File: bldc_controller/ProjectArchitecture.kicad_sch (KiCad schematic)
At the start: 0 parts

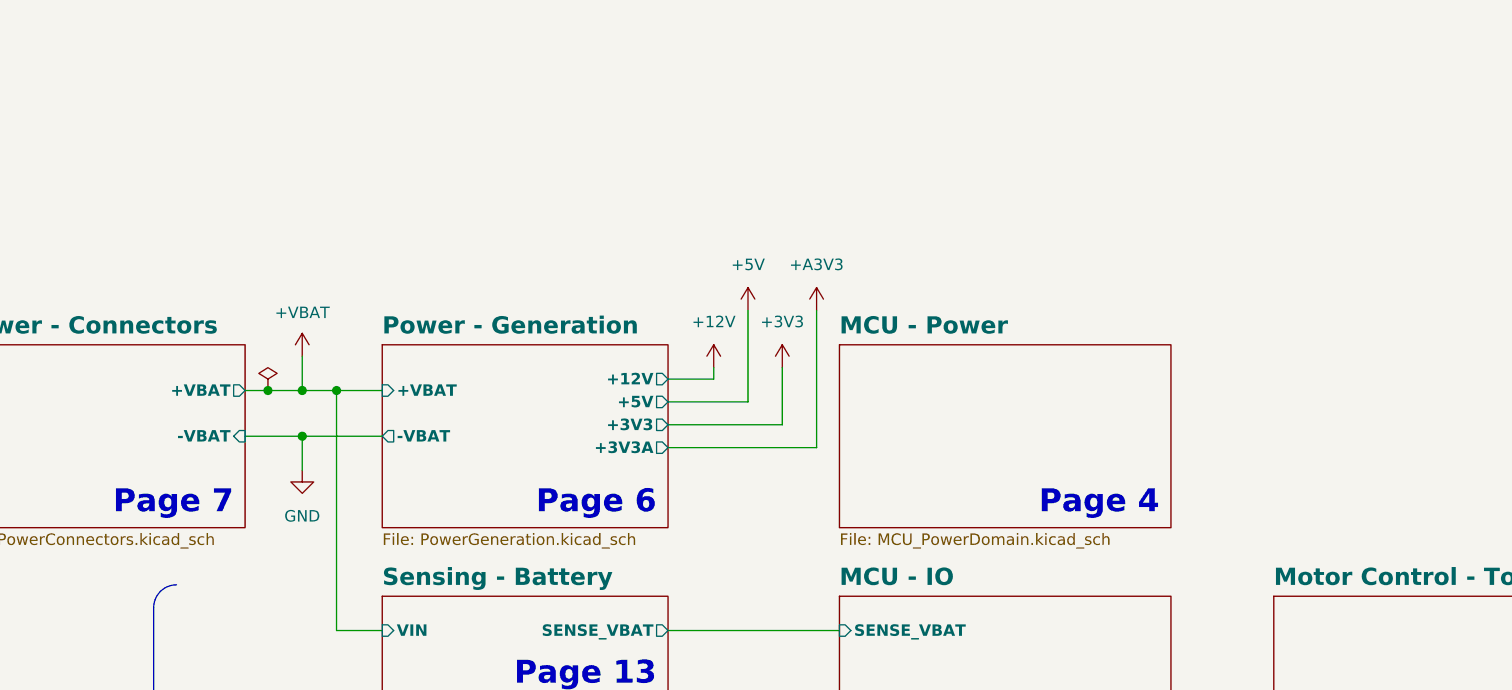
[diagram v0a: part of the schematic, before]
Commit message: added chassis connection to connector MP. Might need to change design rules to be compatible with low-cost PCBWay
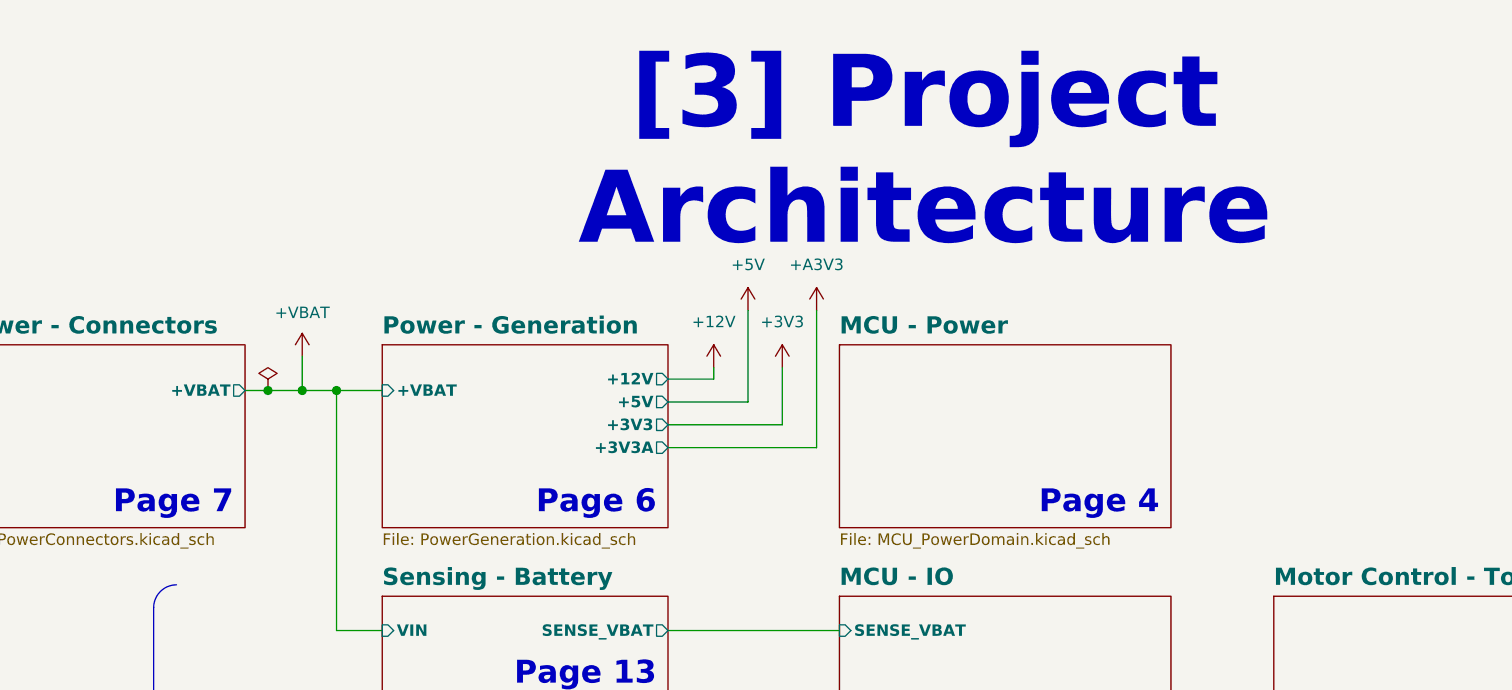
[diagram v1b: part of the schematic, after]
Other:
- sheet Power - Connectors ports: added none; removed -VBAT
- sheet Power - Generation ports: added none; removed -VBAT
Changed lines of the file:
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@@
   (junction (at 195.58 129.54) (diameter 0) (color 0 0 0 0)
-  )
-  (junction (at 140.97 58.42) (diameter 1.016) (color 0 0 0 1)
   )
   (junction (at 195.58 167.64) (diameter 0) (color 0 0 0 0)
@@
     (stroke (width 0) (type default))
   )
-  (wire (pts (xy 140.97 58.42) (xy 149.86 58.42))
-    (stroke (width 0.381) (type default) (color 0 0 0 1))
-  )
   (wire (pts (xy 181.61 101.6) (xy 193.04 101.6))
     (stroke (width 0) (type default))
@@
     (stroke (width 0) (type default))
   )
-  (wire (pts (xy 140.97 58.42) (xy 140.97 62.23))
-    (stroke (width 0.381) (type default) (color 0 0 0 1))
-  )
   (wire (pts (xy 149.86 125.73) (xy 140.97 125.73))
     (stroke (width 0) (type default))
@@
   (bus (pts (xy 181.61 167.64) (xy 195.58 167.64))
     (stroke (width 0) (type default))
-  )
-  (wire (pts (xy 134.62 58.42) (xy 140.97 58.42))
-    (stroke (width 0.381) (type default) (color 0 0 0 1))
   )
   (wire (pts (xy 149.86 134.62) (xy 138.43 134.62))
@@
     (effects (font (size 1.905 1.905) (thickness 0.381) bold (color 0 0 0 1)) (justify right top))
   )
+  (text_box "[3] Project Architecture"
+    (at 144.78 20.32 0) (size 130.81 12.7)
+    (stroke (width -0.0001) (type default))
+    (fill (type none))
+    (effects (font (face "Times New Roman") (size 8 8) (thickness 1.2) bold (color 162 22 34 1)))
+  )
   (text_box "LEDs, version"
     (at 299.085 165.735 0) (size 13.335 7.62)
@@
     )
   )
-  (symbol (lib_id "power:GND") (at 140.97 62.23 0) (unit 1)
-    (in_bom yes) (on_board yes) (dnp no) (fields_autoplaced)
-    (property "Reference" "#PWR03" (at 140.97 68.58 0)
-      (effects (font (size 1.27 1.27)) hide)
-    )
-    (property "Value" "GND" (at 140.97 67.31 0)
-      (effects (font (size 1.27 1.27)))
-    )
-    (property "Footprint" "" (at 140.97 62.23 0)
-      (effects (font (size 1.27 1.27)) hide)
-    )
-    (property "Datasheet" "" (at 140.97 62.23 0)
-      (effects (font (size 1.27 1.27)) hide)
-    )
-    (pin "1")
-    (instances
-      (project "bldc_controller"
-        (path "/0650c7a8-acba-429c-9f8e-eec0baf0bc1c"
-          (reference "#PWR03") (unit 1)
-        )
-        (path "/0650c7a8-acba-429c-9f8e-eec0baf0bc1c/fede4c36-00cc-4d3d-b71c-5243ba232202"
-          (reference "#PWR078") (unit 1)
-        )
-      )
-    )
-  )
   (sheet (at 248.92 173.99) (size 40.64 10.16) (fields_autoplaced)
     (stroke (width 0.1524) (type solid))
@@
       (effects (font (face "Arial") (size 1.27 1.27)) (justify left top))
     )
-    (pin "-VBAT" input (at 134.62 58.42 0)
-      (effects (font (size 1.27 1.27) (thickness 0.254) bold) (justify right))
-    )
     (pin "+VBAT" output (at 134.62 53.34 0)
       (effects (font (size 1.27 1.27) (thickness 0.254) bold) (justify right))
@@
       (effects (font (face "Arial") (size 1.27 1.27)) (justify left top))
     )
-    (pin "-VBAT" output (at 149.86 58.42 180)
-      (effects (font (size 1.27 1.27) (thickness 0.254) bold) (justify left))
-    )
     (pin "+VBAT" input (at 149.86 53.34 180)

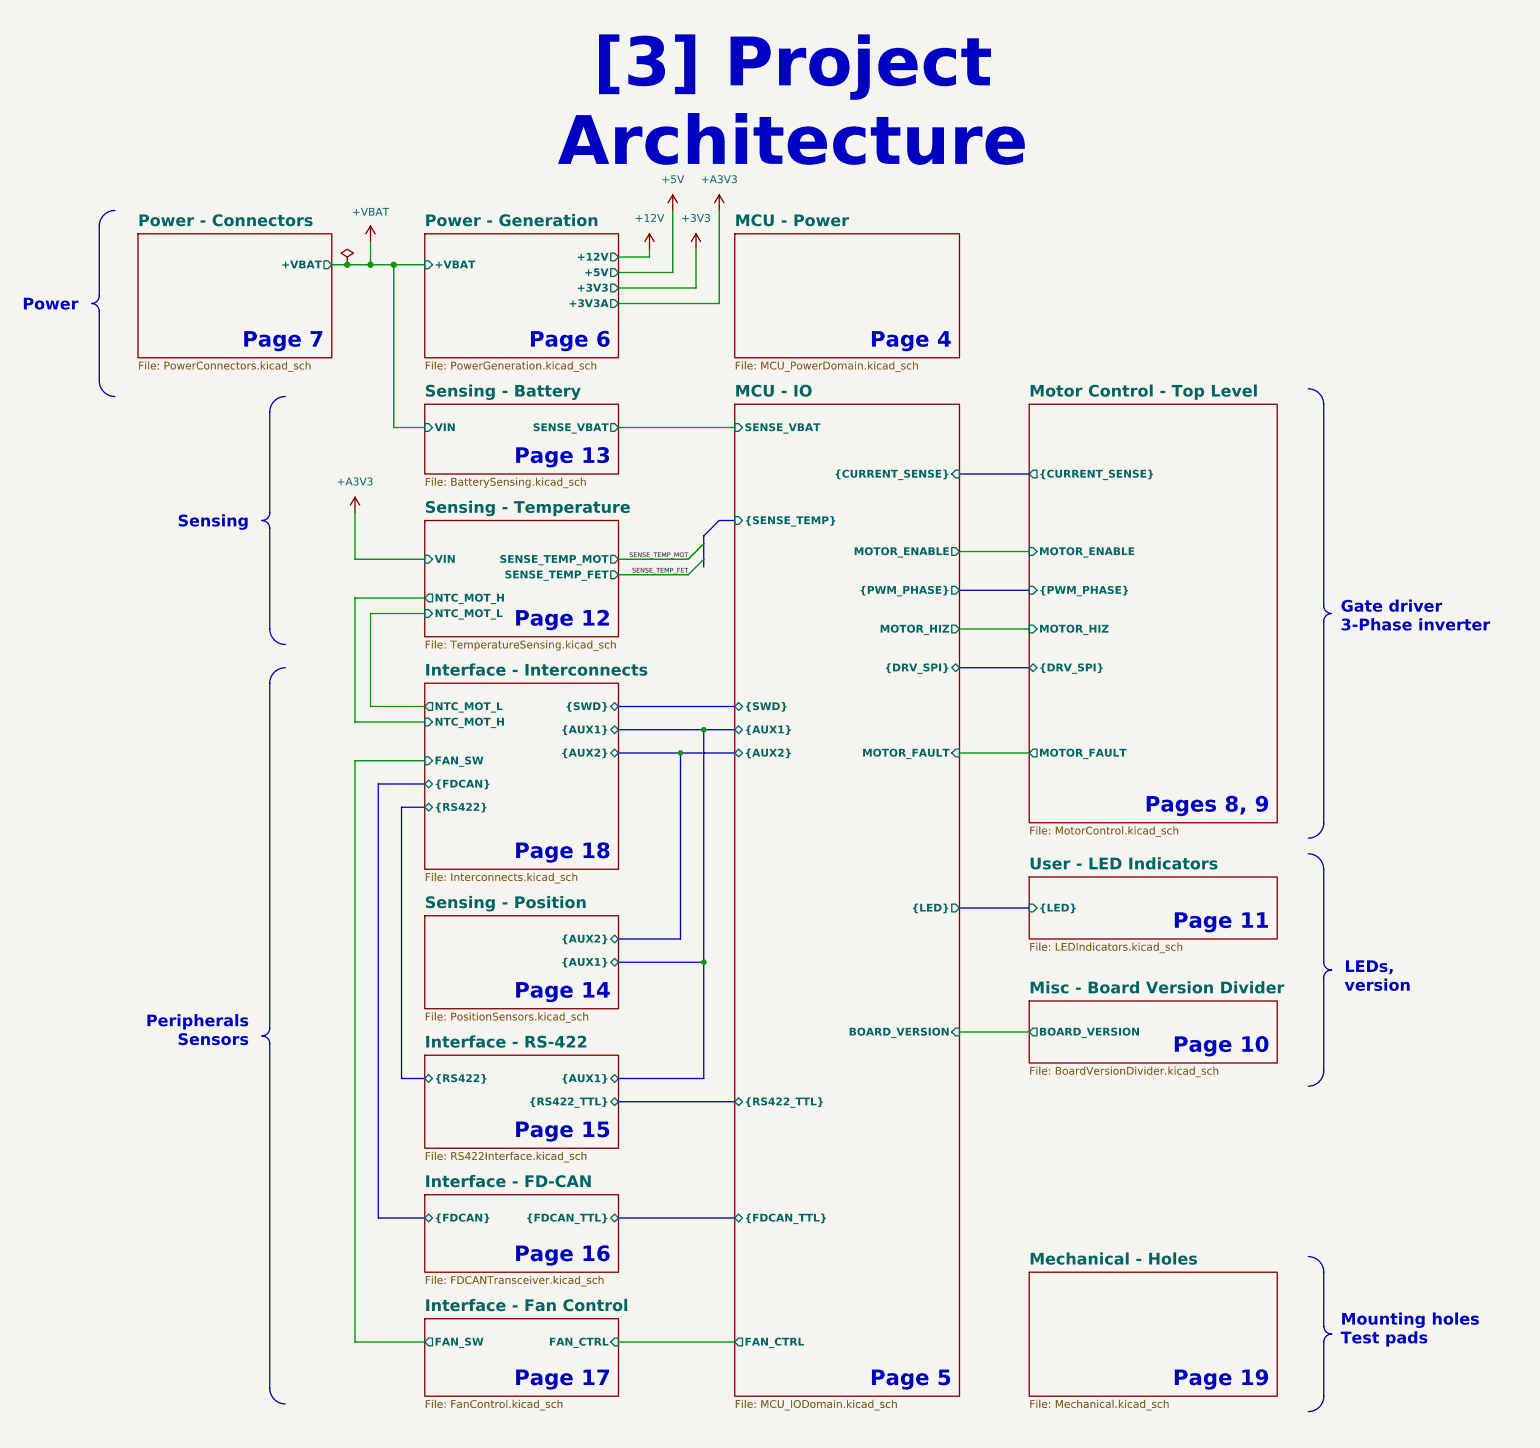
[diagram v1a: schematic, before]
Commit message: Replaced 3v3 buck with WSON package alternative. Will back-annotate components
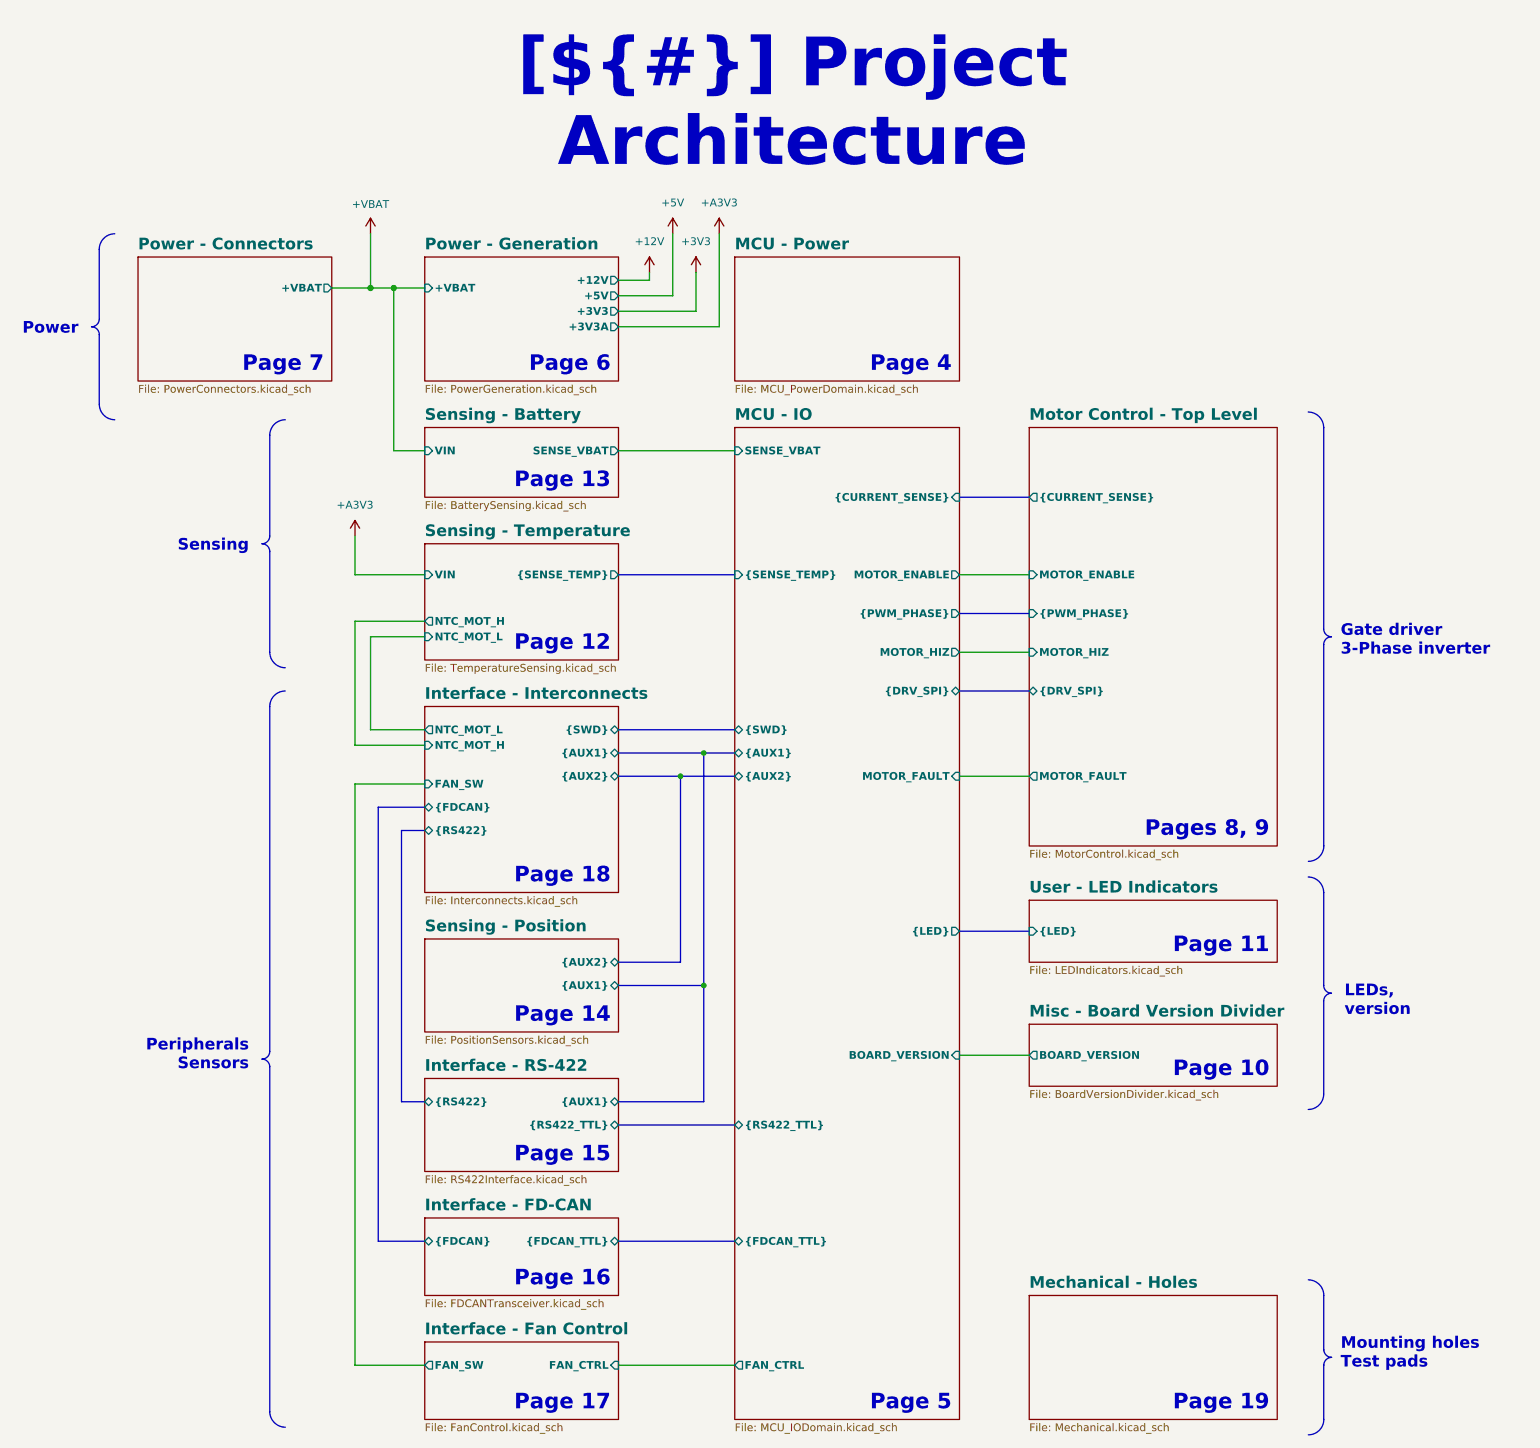
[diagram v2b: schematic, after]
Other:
- sheet Sensing - Temperature ports: added {SENSE_TEMP}; removed SENSE_TEMP_FET, SENSE_TEMP_MOT
- company: EPFL Xplore -> ${COMPANY}
